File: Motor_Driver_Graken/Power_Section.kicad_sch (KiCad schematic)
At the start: 64 parts, among them T1 WE-PPTI_1209, T2 WE-PPTI_1209, T3 WE-PPTI_1209, T4 Transformer_1P_1S, U1 LM2576S-5, U12 SN6501QDBVRQ1, U13 TL431DBZ, U14 SN6501QDBVRQ1, U15 TL431DBZ, U16 SN6501QDBVRQ1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

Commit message: Break Resistor Section
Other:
- note added: "Auxillary power supply for each gate driver and for brake resistor"
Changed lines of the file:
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@@
 	(text "0.5A ≤ ILOAD ≤ 3A, 5.0 V\n"
 		(exclude_from_sim no)
-		(at 144.78 172.974 0)
+		(at 29.718 165.862 0)
 		(effects
 			(font
@@
 	(text "LM2576 \n"
 		(exclude_from_sim no)
-		(at 136.144 166.37 0)
+		(at 21.082 159.258 0)
 		(effects
 			(font
@@
 	(text "8V ≤ VIN ≤ 40V 4.800/4.750 V(Min)\n\n"
 		(exclude_from_sim no)
-		(at 150.114 170.688 0)
+		(at 35.052 163.576 0)
 		(effects
 			(font
@@
 	(text "\n5.200/5.250 V(Max)"
 		(exclude_from_sim no)
-		(at 141.986 175.514 0)
+		(at 26.924 168.402 0)
 		(effects
 			(font
@@
 		)
 	)
+	(text "Auxillary power supply for each gate driver and for brake resistor"
+		(exclude_from_sim no)
+		(at 145.542 165.608 0)
+		(effects
+			(font
+				(size 1.016 1.016)
+			)
+		)
+	)

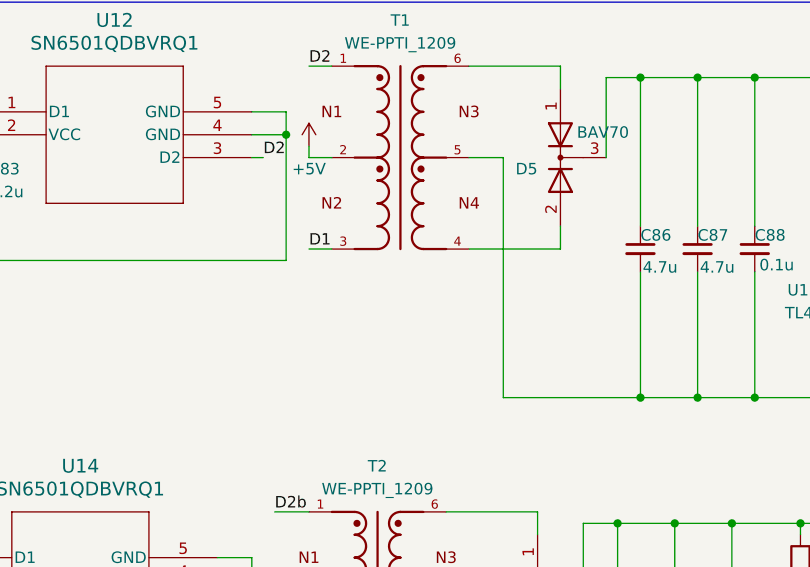
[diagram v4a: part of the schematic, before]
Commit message: adding Simulation Files
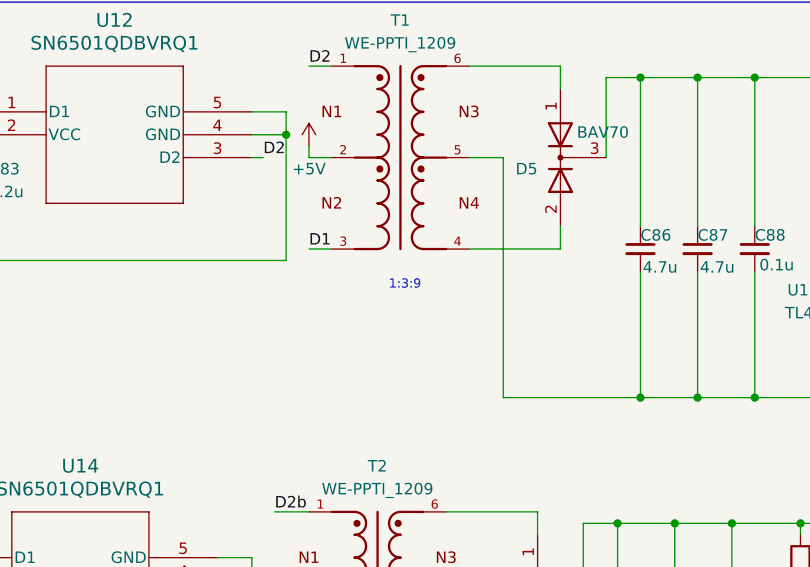
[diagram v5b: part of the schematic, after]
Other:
- note added: "1:3:9"
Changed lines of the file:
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@@
 (kicad_sch
-	(version 20240819)
+	(version 20241004)
 	(generator "eeschema")
 	(generator_version "8.99")
@@
 		(effects
 			(font
+				(size 1.016 1.016)
+			)
+		)
+	)
+	(text "1:3:9"
+		(exclude_from_sim no)
+		(at 189.738 45.974 0)
+		(effects
+			(font
